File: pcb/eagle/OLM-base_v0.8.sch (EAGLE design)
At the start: 33 parts, among them IC1 ATMEGA, IC2 MCP1702-33, IC3 ENC28J60SP, J1 MAGJACK, J2 POWER_JACKPTH, X1 16 MHz, X3 25MHz

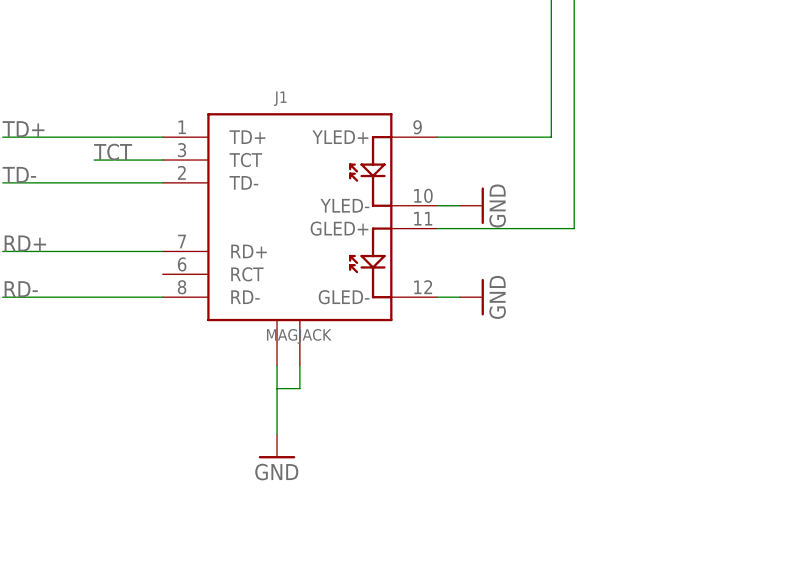
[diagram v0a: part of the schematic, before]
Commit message: changed schematic
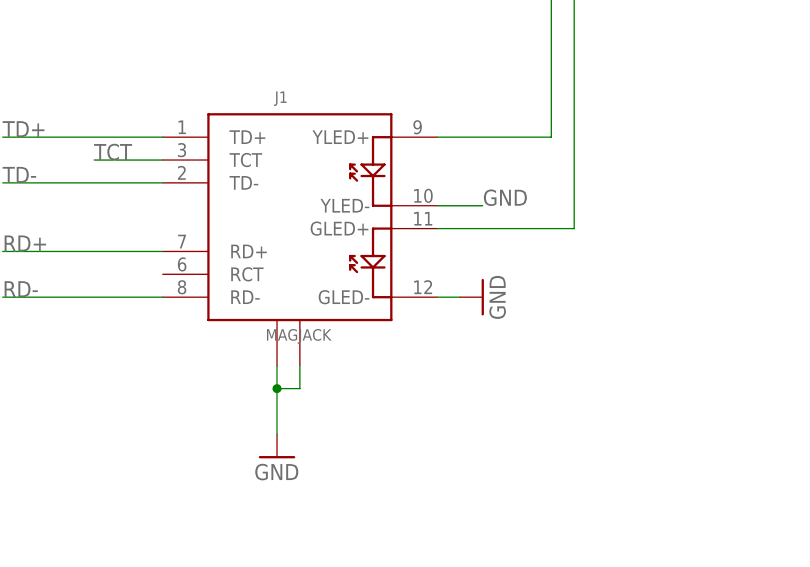
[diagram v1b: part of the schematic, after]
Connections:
- removed net N$36: J1.YLED-
- net GND: now also J1.YLED-
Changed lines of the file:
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@@
 <part name="GND4" library="supply1" deviceset="GND" device=""/>
 <part name="GND1" library="SparkFun" deviceset="GND" device=""/>
-<part name="GND5" library="SparkFun" deviceset="GND" device=""/>
 <part name="J2" library="SparkFun-Connectors" deviceset="POWER_JACK" device="PTH"/>
 </parts>
@@
 <instance part="GND4" gate="1" x="124.46" y="-71.12"/>
 <instance part="GND1" gate="1" x="147.32" y="-53.34" rot="R90"/>
-<instance part="GND5" gate="1" x="147.32" y="-43.18" rot="R90"/>
 <instance part="J2" gate="G$1" x="-12.7" y="-68.58"/>
 </instances>
@@
 <pinref part="J1" gate="G$1" pin="GND1"/>
 <pinref part="J1" gate="G$1" pin="GND2"/>
+<junction x="124.46" y="-63.5"/>
 </segment>
 <segment>
@@
 <junction x="5.08" y="-66.04"/>
 <label x="7.62" y="-73.66" size="1.778" layer="95"/>
+</segment>
+<segment>
+<pinref part="J1" gate="G$1" pin="YLED-"/>
+<wire x1="142.24" y1="-43.18" x2="147.32" y2="-43.18" width="0.1524" layer="91"/>
+<label x="147.32" y="-43.18" size="1.778" layer="95"/>
 </segment>
 </net>
@@
 </segment>
 </net>
-<net name="N$36" class="0">
-<segment>
-<wire x1="144.78" y1="-43.18" x2="142.24" y2="-43.18" width="0.1524" layer="91"/>
-<pinref part="J1" gate="G$1" pin="YLED-"/>
-<pinref part="GND5" gate="1" pin="GND"/>
-</segment>
-</net>
